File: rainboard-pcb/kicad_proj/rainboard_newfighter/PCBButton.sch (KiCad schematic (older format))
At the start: 4 parts

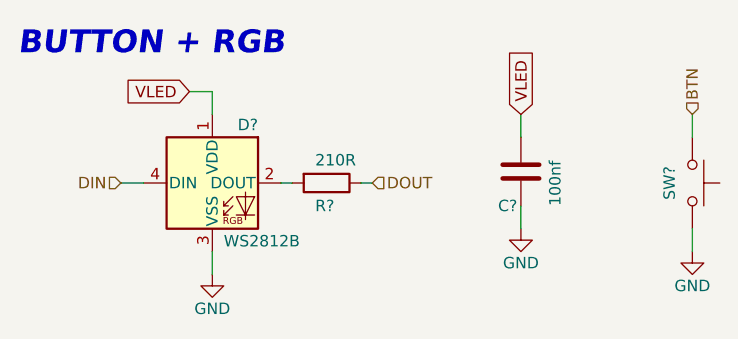
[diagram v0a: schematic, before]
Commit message: Schematic nearly finalized; PCB / footprint started
-Schematic is nearly finished. Needs some footprint associations and verifications.
-A few open questions remain.
-some lib updates to go w/ sch improvements
-
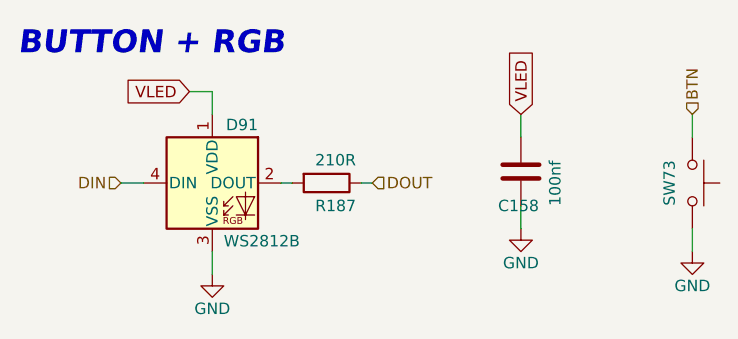
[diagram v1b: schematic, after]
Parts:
- SW17: renamed from SW?; PN (none) -> SANWA-OBSC-CW/W
- gave numbers to parts that had none: 3
